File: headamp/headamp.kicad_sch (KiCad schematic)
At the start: 77 parts, among them J1 MAINS 230V, K1 9V, SW1 ON/OFF, SW2 S2 wokal, SW202 S2 wokal (P), T1 OPT SE 5k:80R (>=25H, 45mA), T201 OPT SE 5k:80R (>=25H, 45mA), T301 EI84 100VA: 230V : 250V/0,15A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, U1 ECC82, U2 EL84 (trioda), U202 EL84 (trioda), U301 LD1085 (LDO)

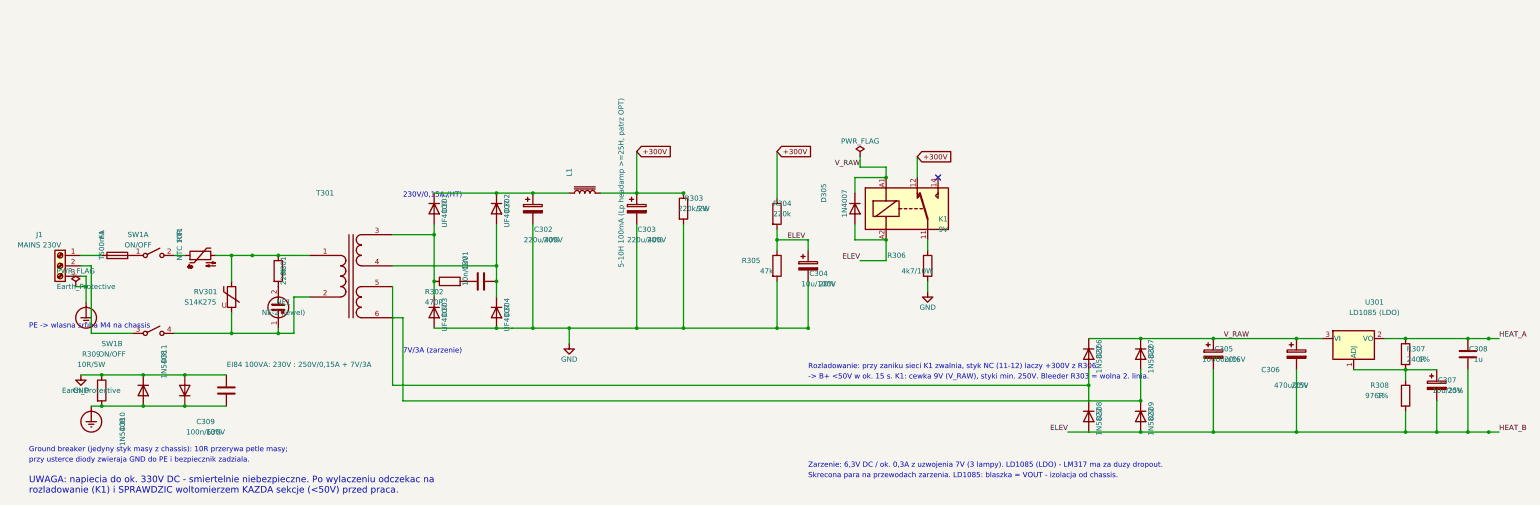
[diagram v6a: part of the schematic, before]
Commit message: headamp: Etap 6 - estetyka schematu (pola ref/value/tolerance)
Przeglad renderu (Konnect render_schematic_png) wykazal liczne
nakladajace sie pola Reference/Value/Tolerance w nowych sekcjach
(kanal P, zasilacz). Poprawki w gen.py:
- domyslne polozenie pol (gdy 'fields' nie podaje jawnie) rozszerzone
  o trzeci wiersz (Tolerance) zamiast zgadywania z vpos - usuwa
  nachodzenie value/tolerance na diodach mostka i duzych kondensatorach
  (C305 10000u, C306, C307, C308, R307, R308).
- jawne fields dla C302/C303/R303/C304/L1 (tolerancja/wartosc rozsuniete
  od kolumny R303 i od dlugiego opisu L1 - skrocony do "5-10H 100mA",
  szczegol w osobnym text()).
- F1 przesuniety nad linie LR (nie kolidowal juz z SW1A).
- PE: PWR_FLAG i Earth_Protective rozsuniete od numerow pinow J1
  (dodatkowo pe() dostal parametr rot, zeby Value nie nachodzilo na GND
  w ground breakerze).
- ground breaker: pola R309/D310/D311/C309 przesuniete blisko elementow
  (nie kolidowaly z SW1B).
- R301/NE1: etykieta NE1 przesunieta w prawo (nie nachodzila na kolumne
  R301).
- adnotacja "230V/0,15A (HT)" / "7V/3A" przesunieta w lewo (nie
  nachodzila na D301-304).

Regeneracja idempotentna (dwa uruchomienia identyczne), check.py OK
(50 sieci), ERC 0 bledow / 5 oczekiwanych ostrzezen (bez zmian wobec
Etapu 5b). Otwarte: rzad grzania (3 lampy) pozostaje ciasny wizualnie -
zanotowane w docs jako TODO.

Co-Authored-By: Claude Sonnet 5 <noreply@anthropic.com>
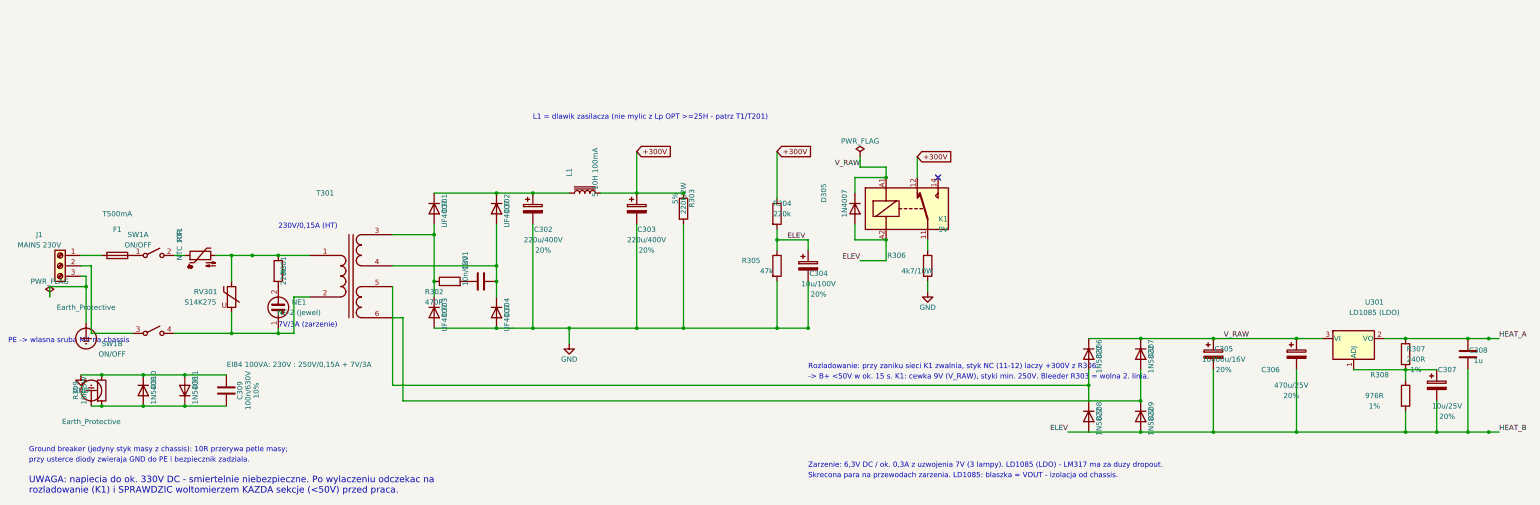
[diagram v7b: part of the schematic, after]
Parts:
- L1: value 5-10H 100mA (Lp headamp >=25H, patrz OPT) -> 5-10H 100mA
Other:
- note added: "L1 = dlawik zasilacza (nie mylic z Lp OPT >=25H - patrz T1/T201)"

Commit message: headamp: layout w ramkach modulow, polaczenia drutami (hybryda), zarzenie jako etykiety
Etap A (DECYZJE 2026-09-08, docs/PROJEKT-HEADAMP.md nastepuje w Etapie C):
- B+ (+300V): zamiast global_label - realne druty + wspolna magistrala
  pionowa BUS_X=245,11mm laczaca oba kanaly (korytarze nad modulami,
  y=80,01/185,42) z zasilaczem (CLC, R304/elewacja, K1). GND/PE zostaja
  symbolami power (bez zmian).
- Zarniki lamp NIE SA RYSOWANE: usuniete unity grzania ECC82 (U1 unit3),
  EL84 (U2/U202 unit2) wraz z drutami/etykietami po stronie lamp. Blok
  zarzenia w zasilaczu (LD1085) konczy sie etykietami lokalnymi HEAT_A/
  HEAT_B + adnotacja tekstowa z mapowaniem pinow. PWR_FLAG na HEAT_B
  przeniesiony do tego bloku (jedyne miejsce gdzie ta siec istnieje).
- Layout w ramkach (rectangle na arkuszu): WEJSCIE, KANAL L, KANAL P,
  WYJSCIE (dwie ostatnie na razie puste - Etap B), SIEC/ZASILACZ B+/
  ZARZENIE w dolnym rzedzie. Paper zostaje A2 (tresc ~400x428mm).
- check.py: usuniete asercje okablowania zarnikow po stronie lamp
  (U1.4/5/9, U2.4/5, U202.4/5 - juz nie istnieja w netliscie); HEAT_A/
  HEAT_B sprawdzane teraz tylko po stronie zasilacza (U301/R307/R308/
  C307/C308).

ERC: 0 bledow oczekiwanych typem (missing_unit x3, isolated_pin_label
IN/OUT x4 - do Etapu B, multiple_net_names ELEV/HEAT_B) + 3 bledy
missing_power_pin (U1/U2/U202) - KONSEKWENCJA usuniecia unitow grzania:
ich piny grzania sa typu power_in w bibliotece Valve, KiCad flaguje
nieumieszczony unit z pinami power_in jako error, nie tylko warning
(nowa informacja, brief zakladal same warningi). Nie da sie tego wylaczyc
bez zmiany erc rule_severities w headamp.kicad_pro (plik poza zakresem -
nie ruszac/nie commitowac). Do decyzji uzytkownika w docs (Etap C).

Co-Authored-By: Claude Sonnet 5 <noreply@anthropic.com>
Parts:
- removed unit 3 of U1
- removed unit 2 of U2
- removed unit 2 of U202
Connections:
- net +300V: no longer names the net of C303.1, K1.12, L1.2, R205.2, R303.1, R304.1, R5.2, T1.1 (AA), T201.1 (AA)
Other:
- note added: "EL84 (x2) pin 4 -> HEAT_A, pin 5 -> HEAT_B. Zarniki NIE sa rysowane (patrz docs)."
- note added: "KANAL L: 1/2 ECC82 -> EL84 (trioda) -> OPT"
- note added: "KANAL P: 1/2 ECC82 -> EL84 (trioda) -> OPT"
- note added: "SIEC 230V + ground breaker"
- note added: "WEJSCIE: gniazda RCA, crossfeed S1, glosnosc RV1"
- note added: "WYJSCIE: jack 6,3 mm"
- note added: "ZARZENIE 6,3V DC (LD1085, elewacja ELEV)"
- note added: "ZASILACZ B+ 300V (CLC) + rozladowanie K1"
- note added: "Zarzenie do lamp (skrecona para): ECC82 piny 4+5 -> HEAT_A, pin 9 -> HEAT_B;"
